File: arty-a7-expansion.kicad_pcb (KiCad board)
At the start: 4 copper layers, 109.4 x 40 mm, 61 parts, among them IC1 TPD8S009DSMR, J2 1140084168, J4 685119134923, J5 UE27AC54100, U1 TPS61232DRCT, U2 MAX3421EEHJ, Y1 KX-7_12.MHz

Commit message: Cleanup
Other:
- board text removed: "Rev.1.0 09/2019"
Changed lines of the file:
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@@
-(kicad_pcb (version 20171130) (host pcbnew 5.1.4+dfsg1-1~bpo9+1)
+(kicad_pcb (version 20171130) (host pcbnew 5.1.5+dfsg1-2~bpo10+1)
   (general
     (thickness 1.6)
@@
   (layers
     (0 F.Cu signal)
-    (1 In1.Cu signal hide)
-    (2 In2.Cu signal hide)
+    (1 In1.Cu signal)
+    (2 In2.Cu signal)
     (31 B.Cu signal)
-    (32 B.Adhes user hide)
-    (33 F.Adhes user hide)
-    (34 B.Paste user hide)
-    (35 F.Paste user hide)
-    (36 B.SilkS user hide)
+    (32 B.Adhes user)
+    (33 F.Adhes user)
+    (34 B.Paste user)
+    (35 F.Paste user)
+    (36 B.SilkS user)
     (37 F.SilkS user)
-    (38 B.Mask user hide)
-    (39 F.Mask user hide)
-    (40 Dwgs.User user hide)
-    (41 Cmts.User user hide)
+    (38 B.Mask user)
+    (39 F.Mask user)
+    (40 Dwgs.User user)
+    (41 Cmts.User user)
     (42 Eco1.User user)
     (43 Eco2.User user)
     (44 Edge.Cuts user)
     (45 Margin user)
-    (46 B.CrtYd user hide)
-    (47 F.CrtYd user hide)
+    (46 B.CrtYd user)
+    (47 F.CrtYd user)
     (48 B.Fab user)
-    (49 F.Fab user hide)
+    (49 F.Fab user)
   )
   (setup
@@
     (effects (font (size 1 1) (thickness 0.25)))
   )
-  (gr_text "Rev.1.0 09/2019" (at 164.5605 98.4135) (layer F.Mask)
+  (gr_text "Rev.1.1 02/2020" (at 164.5605 98.4135) (layer F.Mask)
     (effects (font (size 0.8 0.8) (thickness 0.2)))
   )

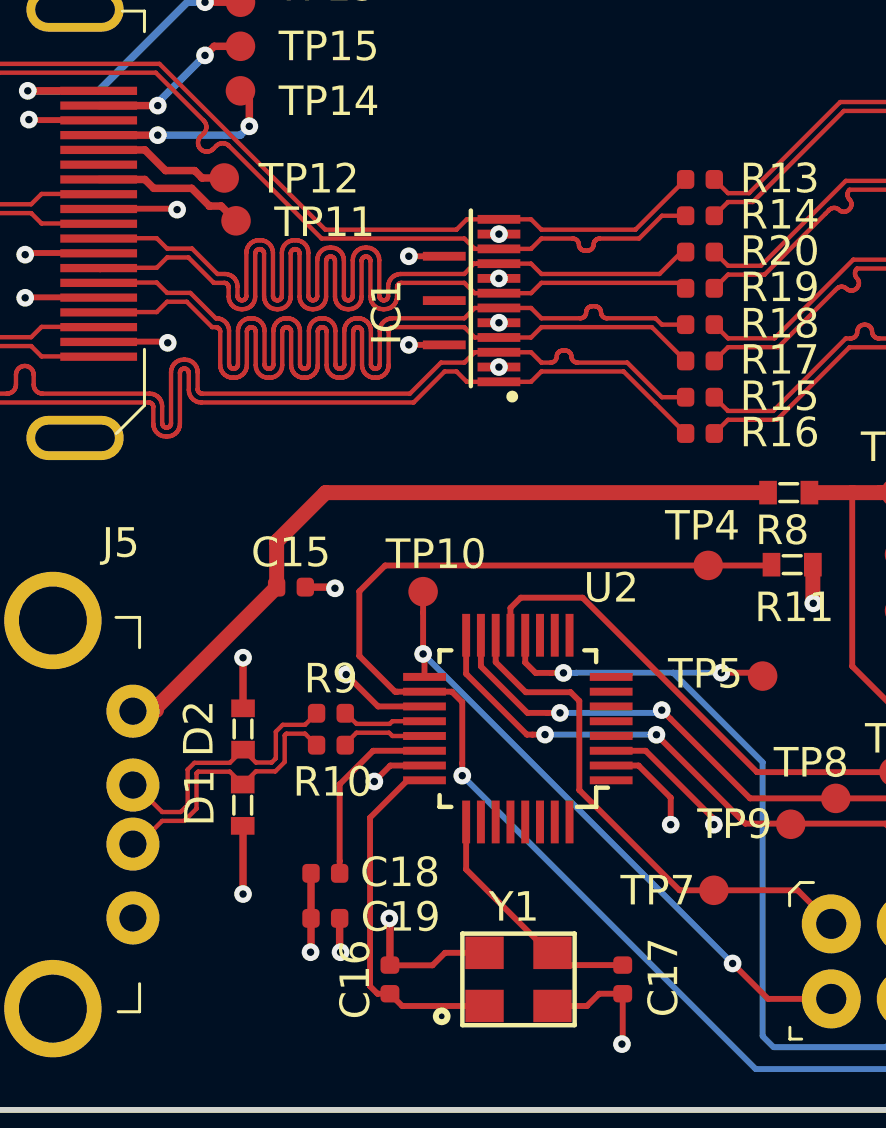
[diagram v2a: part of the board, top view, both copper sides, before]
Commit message: Updated U1 MPN, updated layout around IC1
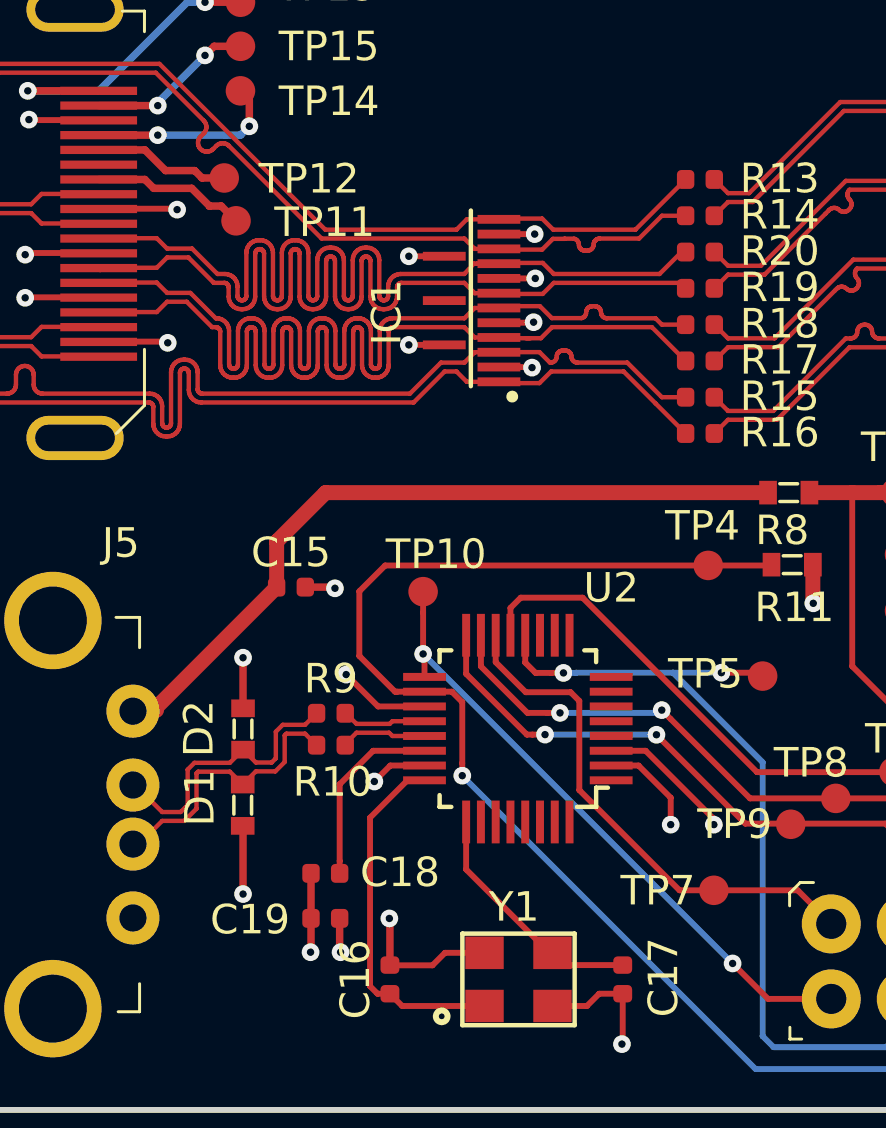
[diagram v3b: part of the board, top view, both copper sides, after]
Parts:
- turned C19 to 0 degrees
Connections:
- net Net-(C16-Pad1) renamed /XI
- net Net-(C17-Pad1) renamed /XO
- C19 pad 1: +3V3 -> GND
- C19 pad 2: GND -> +3V3
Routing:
- net GND: track 63.1 -> 67.8 mm

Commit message: Minor changes
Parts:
- added R23: R_0R_0603, arty-a7-expansion-footprints:0603-res, F.Cu at (124.6, 108.3)
- C1, C11, C15, C16, C17, C18, C19: footprint HDMI_SD_expansion-footprints:0402-cap -> arty-a7-expansion-footprints:0402-cap
- C10, C12, C13, C14: footprint HDMI_SD_expansion-footprints:0603-cap -> arty-a7-expansion-footprints:0603-cap
- D1, D2: footprint HDMI_SD_expansion-footprints:PGB1010603MR -> arty-a7-expansion-footprints:PGB1010603MR
- IC1: footprint HDMI_SD_expansion-footprints:R-PDSO-N15 -> arty-a7-expansion-footprints:R-PDSO-N15
- J2: footprint HDMI_SD_expansion-footprints:MicroSD_1140084168 -> arty-a7-expansion-footprints:MicroSD_1140084168
- J4: footprint HDMI_SD_expansion-footprints:HDMI_A_Female_685119134923 -> arty-a7-expansion-footprints:HDMI_A_Female_685119134923
- J5: footprint HDMI_SD_expansion-footprints:USB_A_Female_UE27AC54100 -> arty-a7-expansion-footprints:USB_A_Female_UE27AC54100
- L1: footprint HDMI_SD_expansion-footprints:XFL4020-102MEB -> arty-a7-expansion-footprints:XFL4020-102MEB
- R1, R11, R2, R3, R4, R5, R6, R7, R8: footprint HDMI_SD_expansion-footprints:0603-res -> arty-a7-expansion-footprints:0603-res
- R10, R12, R13, R14, R15, R16, R17, R18, R19, R20, R9: footprint HDMI_SD_expansion-footprints:0402-res -> arty-a7-expansion-footprints:0402-res
- TP1, TP10, TP11, TP12, TP13, TP14, TP15, TP2, TP3, TP4, TP5, TP6, TP7, TP8, TP9: footprint HDMI_SD_expansion-footprints:Testpoint_smd_1mm -> arty-a7-expansion-footprints:Testpoint_smd_1mm
- U1: footprint HDMI_SD_expansion-footprints:VSON-10-1EP_3x3mm -> arty-a7-expansion-footprints:VSON-10-1EP_3x3mm
- U2: footprint HDMI_SD_expansion-footprints:TQFP-32_5x5mm -> arty-a7-expansion-footprints:TQFP-32_5x5mm
- Y1: footprint HDMI_SD_expansion-footprints:KX-7 -> arty-a7-expansion-footprints:KX-7
- moved C14 8.80 mm to (133.5, 102.9), turned to 90 degrees
- moved C10 6.28 mm to (143.1, 109.3)
- moved C12 3.67 mm to (131.7, 102.9)
- moved C13 3.64 mm to (129.9, 102.9)
- moved L1 1.88 mm to (139.8, 107.2)
- moved TP3 1.48 mm to (128.4, 103.6)
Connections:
- net /D+ renamed Net-(R10-Pad2)
- net /D- renamed Net-(R9-Pad2)
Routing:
- net +3V3: track 42.9 -> 35.5 mm, vias 15 -> 19
- net Net-(L1-Pad1): track 6.10 -> 0.25 mm, vias 0 -> 4
- net /RST_USB: track 29.0 -> 30.3 mm
- net Net-(C12-Pad1): track 29.6 -> 28.3 mm
- added copper zone on F.Cu, net +3V3
- added copper zone on F.Cu, net Net-(L1-Pad1)
